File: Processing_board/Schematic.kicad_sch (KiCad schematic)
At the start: 28 parts, among them J12 Conn_01x08_Pin, J13 Conn_01x08_Pin, J15 Conn_01x06_Pin, J16 Conn_01x03_Pin, J17 Conn_01x03_Pin, J18 Conn_01x02_Pin, J21 Conn_01x02_Pin, SW3 TL3305BF100QG, SW4 TL3305BF100QG, U13 STM32WBA63CIU6

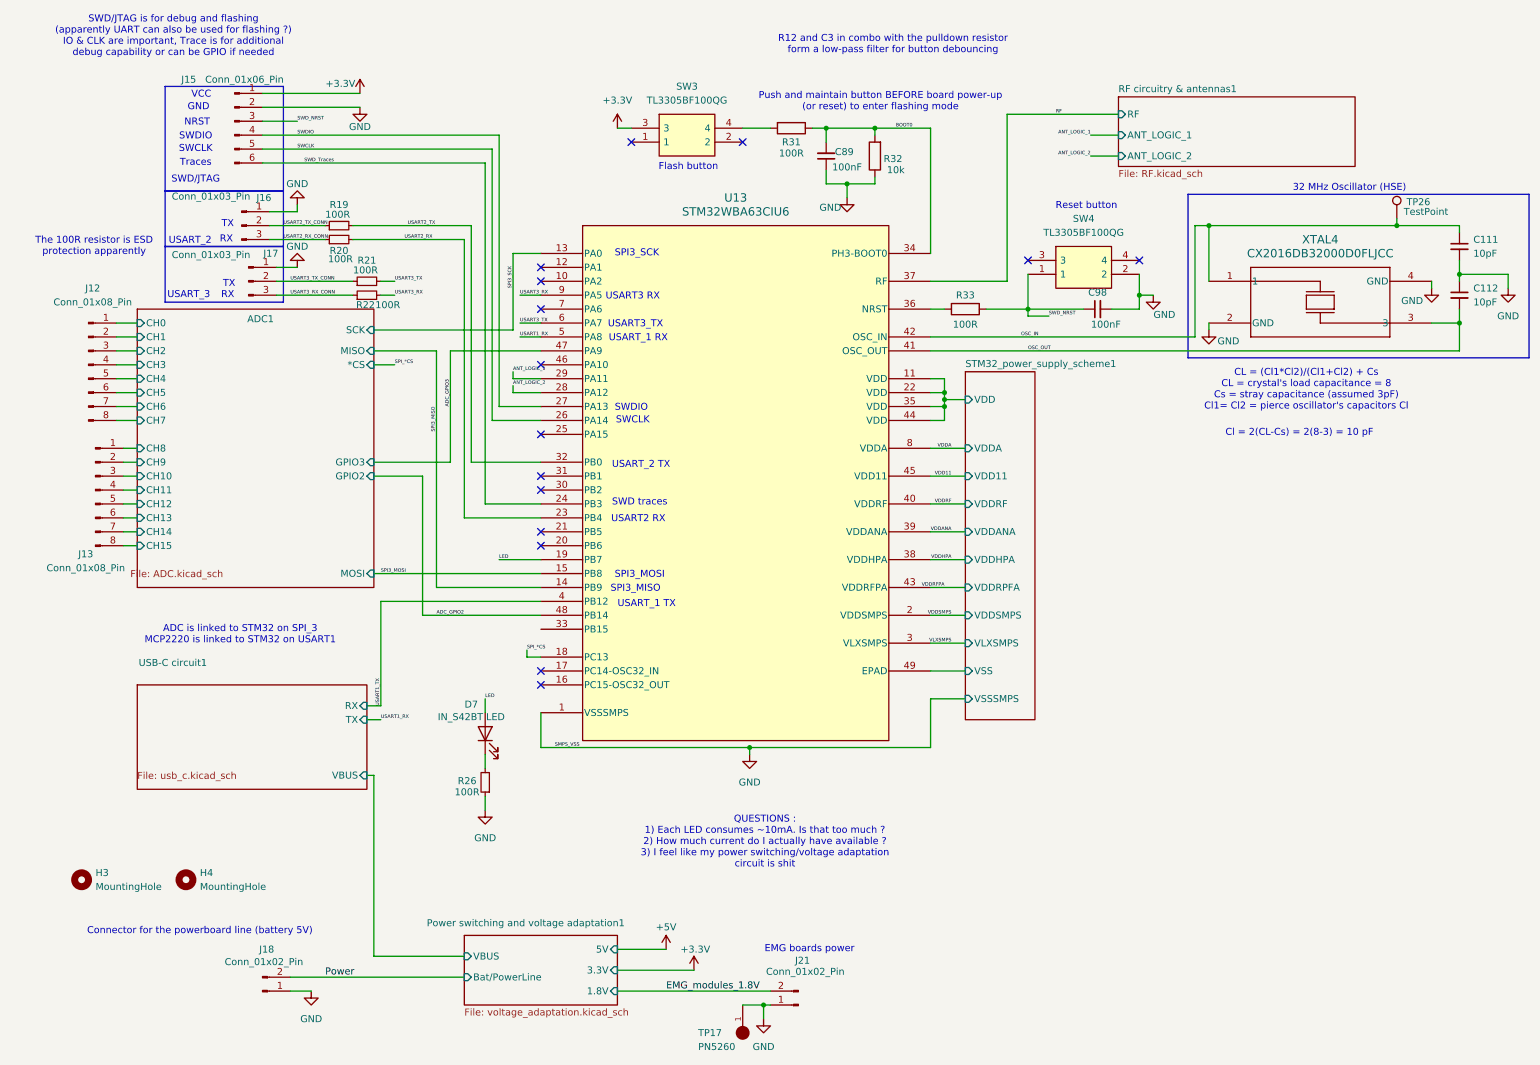
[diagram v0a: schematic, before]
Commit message: had to rename all components on the PCB to match the schematic
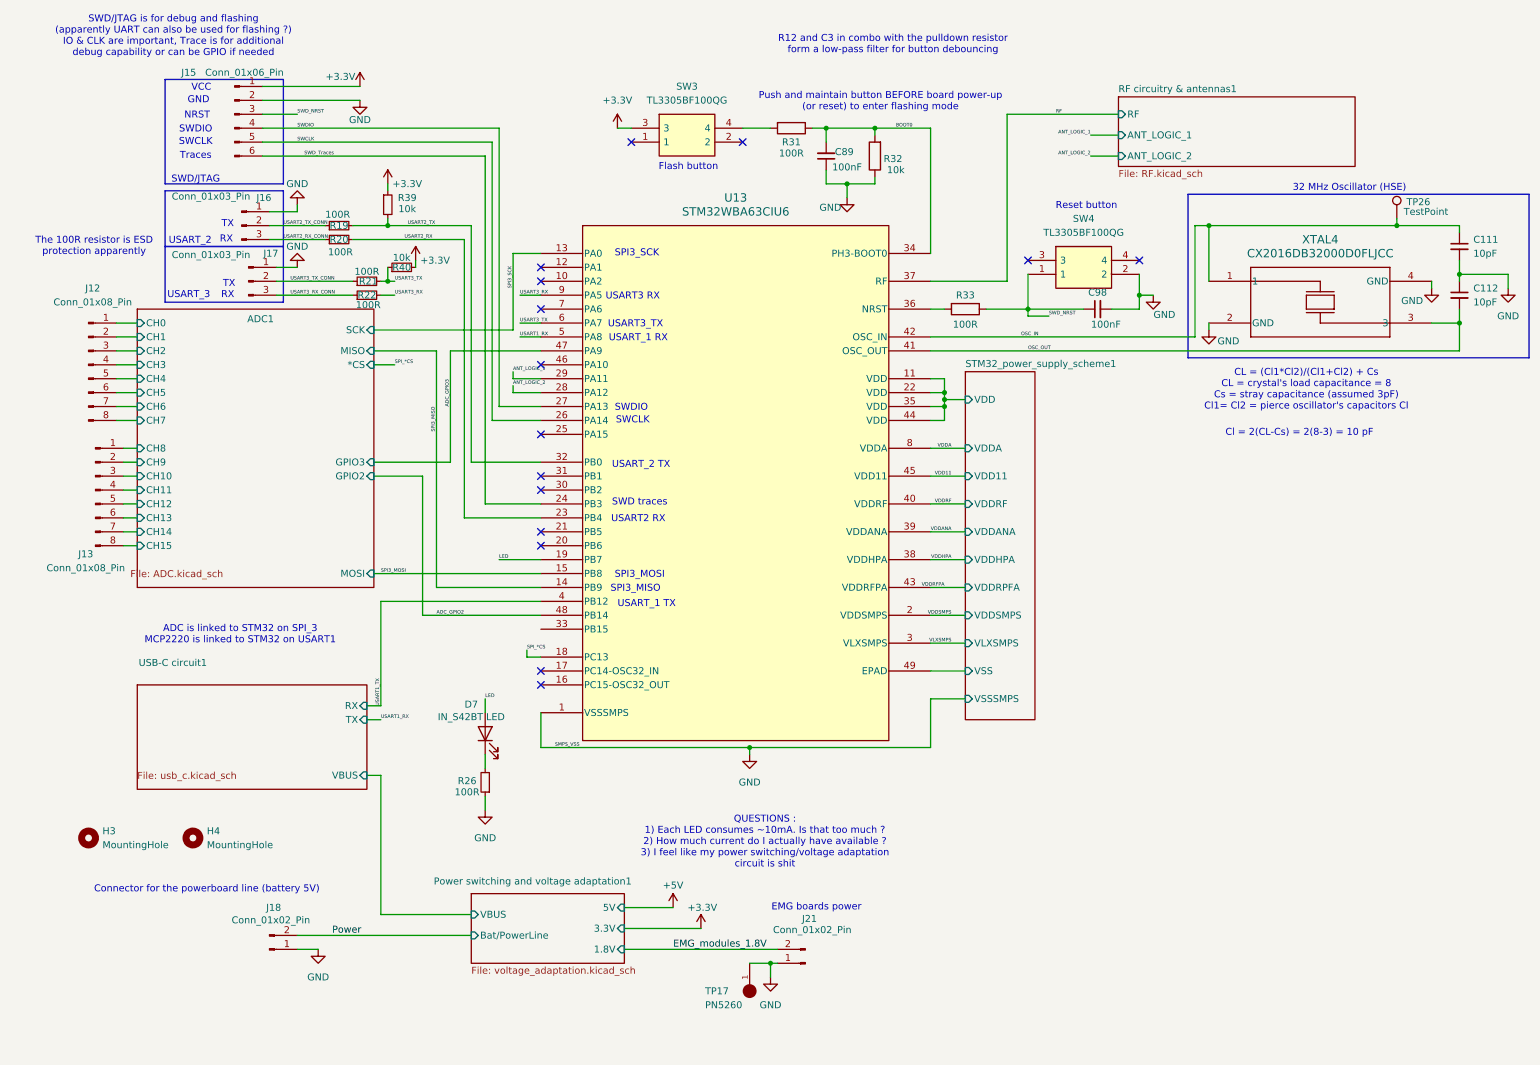
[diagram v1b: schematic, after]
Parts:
- added R39, R40: 10k, Resistor_SMD:R_0402_1005Metric, symbol Device:R_Small
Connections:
- net +3.3V: now also R39.1, R40.2
- net USART2_TX: now also R39.2
- net USART3_TX: now also R40.1
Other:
- moved on the sheet: H3, H4, J15, J18, J21, TP17
